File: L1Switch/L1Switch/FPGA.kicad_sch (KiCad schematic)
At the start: 34 parts, among them J11 Conn_01x06_Male, U1 XC7A35T-FTG256, X1 LFSPXO076034CUTT

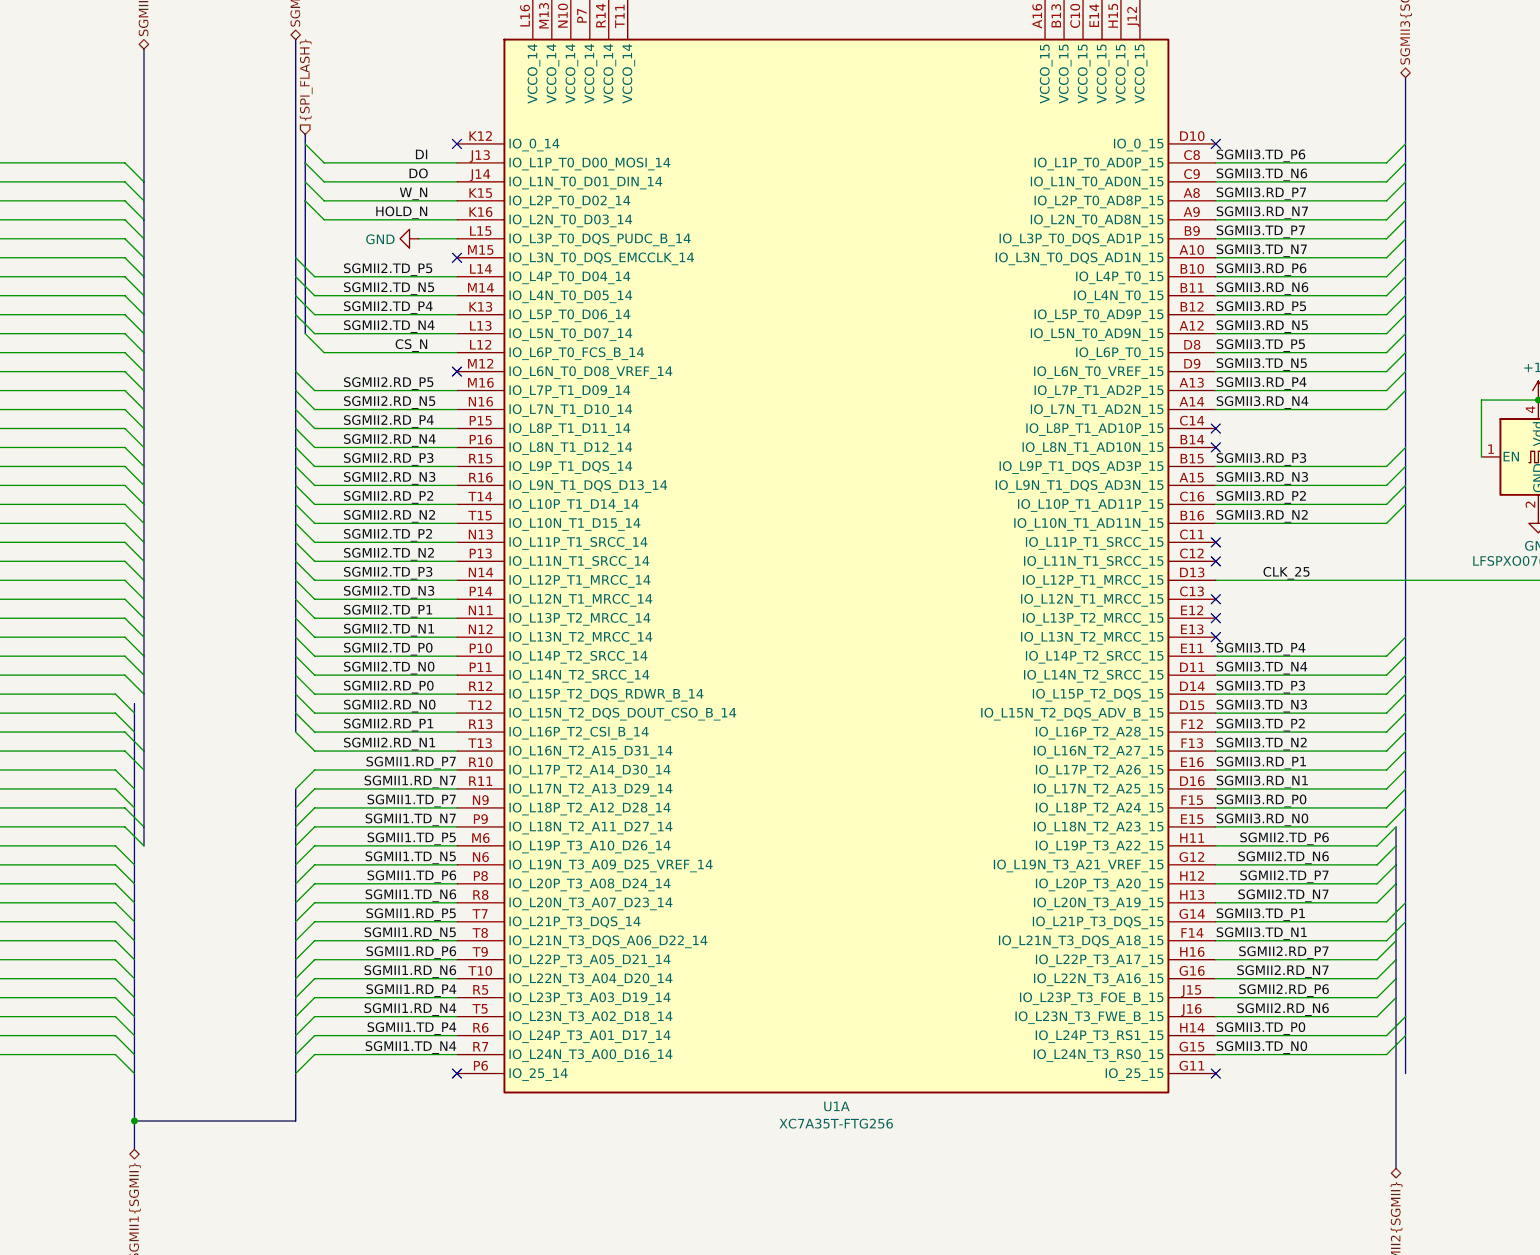
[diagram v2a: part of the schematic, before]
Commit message: Add PWR_FLAG to clean up ERC errors about undriven nets. Change R269 from 100K0 to 10K0.
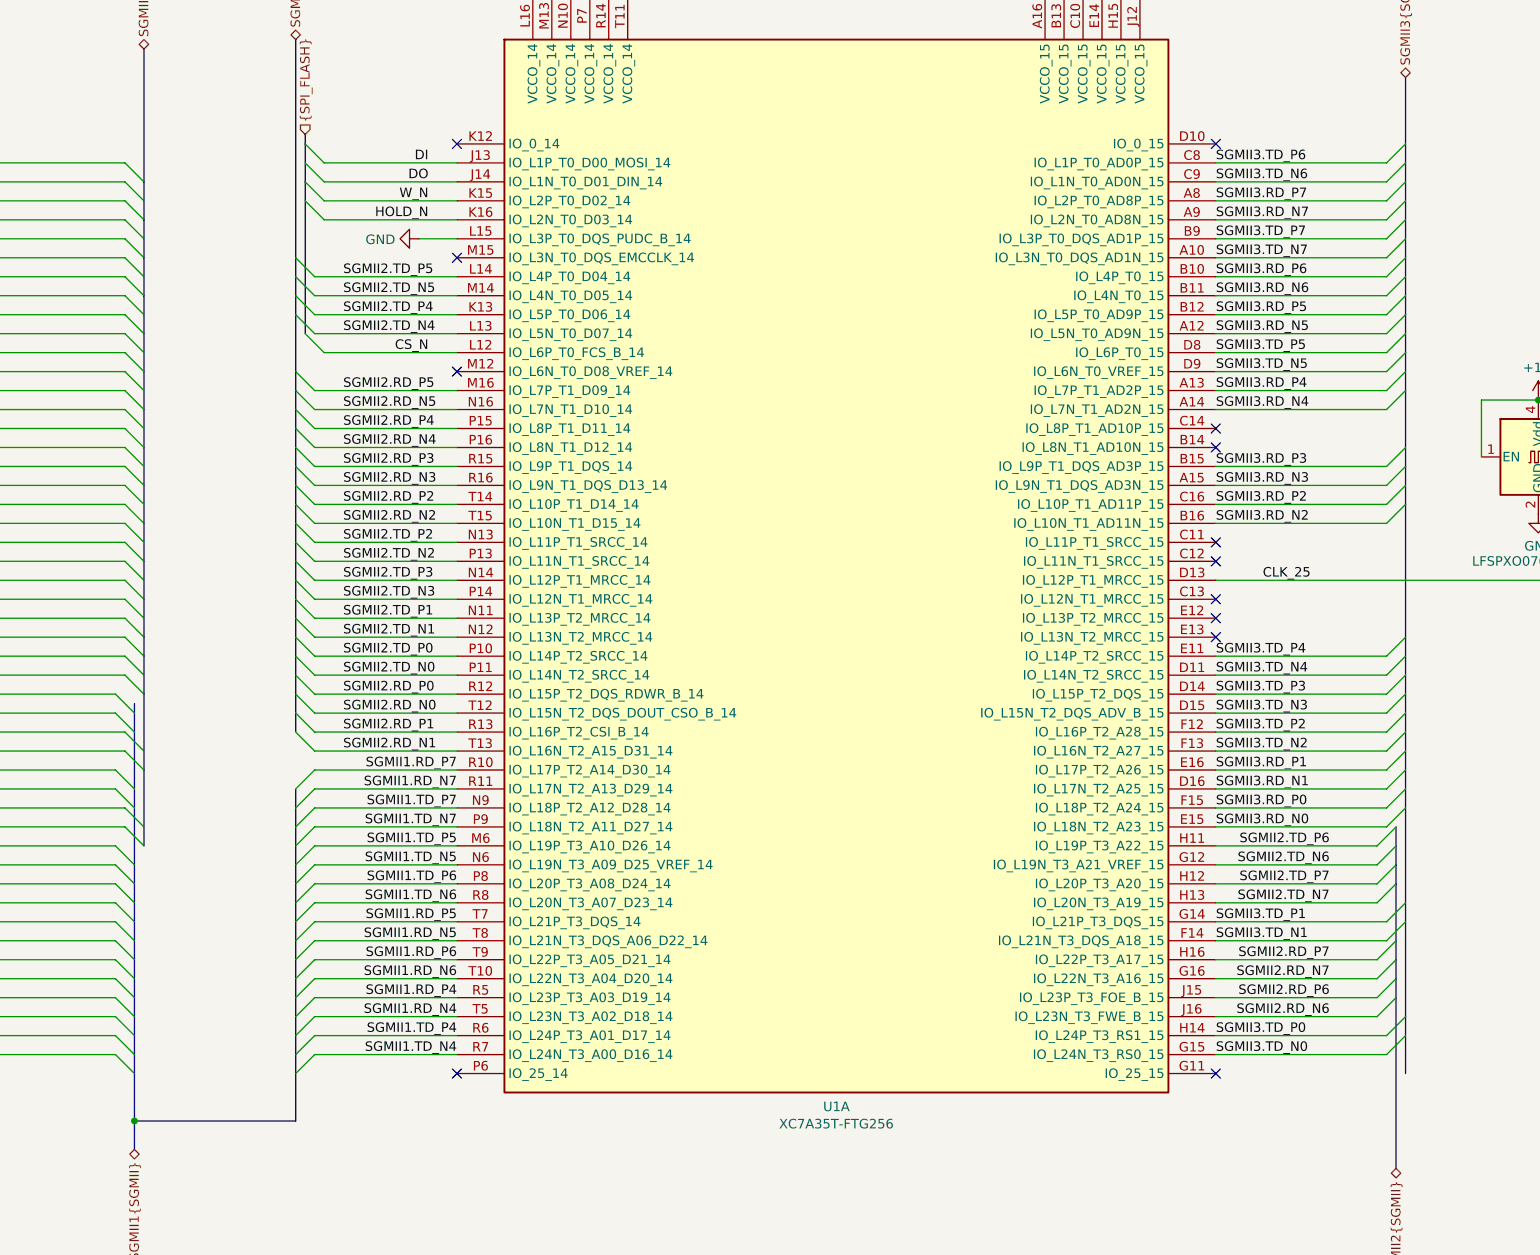
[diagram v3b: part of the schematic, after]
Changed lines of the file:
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@@
-(kicad_sch (version 20200608) (host eeschema "5.99.0-unknown-1973153~101~ubuntu20.04.1")
+(kicad_sch (version 20200608) (host eeschema "(5.99.0-1946-g60915fbc7)")
   (page 1 12)
   (paper "B")
@@
   (junction (at 414.02 125.73))
   (junction (at 213.36 198.12))
-  (no_connect (at 358.14 105.41))
-  (no_connect (at 358.14 123.19))
+  (no_connect (at 256.54 191.77))
+  (no_connect (at 256.54 82.55))
+  (no_connect (at 76.2 115.57))
   (no_connect (at 358.14 191.77))
-  (no_connect (at 76.2 102.87))
-  (no_connect (at 76.2 115.57))
-  (no_connect (at 177.8 67.31))
-  (no_connect (at 358.14 130.81))
-  (no_connect (at 256.54 67.31))
-  (no_connect (at 46.99 114.3))
-  (no_connect (at 358.14 133.35))
-  (no_connect (at 76.2 107.95))
-  (no_connect (at 358.14 120.65))
-  (no_connect (at 256.54 97.79))
-  (no_connect (at 177.8 191.77))
-  (no_connect (at 256.54 191.77))
-  (no_connect (at 76.2 105.41))
   (no_connect (at 46.99 116.84))
   (no_connect (at 358.14 128.27))
+  (no_connect (at 76.2 107.95))
+  (no_connect (at 256.54 67.31))
+  (no_connect (at 358.14 123.19))
+  (no_connect (at 358.14 105.41))
+  (no_connect (at 177.8 191.77))
+  (no_connect (at 177.8 67.31))
+  (no_connect (at 46.99 124.46))
+  (no_connect (at 358.14 120.65))
   (no_connect (at 358.14 67.31))
-  (no_connect (at 46.99 124.46))
-  (no_connect (at 256.54 82.55))
+  (no_connect (at 46.99 114.3))
+  (no_connect (at 256.54 97.79))
   (no_connect (at 358.14 107.95))
+  (no_connect (at 358.14 130.81))
+  (no_connect (at 76.2 105.41))
+  (no_connect (at 358.14 133.35))
+  (no_connect (at 76.2 102.87))
   (bus_entry (at 210.82 140.97) (size 2.54 2.54))
   (bus_entry (at 210.82 143.51) (size 2.54 2.54))
@@
     (stroke (width 0) (type solid) (color 0 0 0 0))
   )
-  (bus (pts (xy 213.36 184.15) (xy 213.36 189.23))
-    (stroke (width 0) (type solid) (color 0 0 0 0))
-  )
-  (bus (pts (xy 213.36 189.23) (xy 213.36 198.12))
+  (bus (pts (xy 213.36 184.15) (xy 213.36 186.69))
+    (stroke (width 0) (type solid) (color 0 0 0 0))
+  )
+  (bus (pts (xy 213.36 186.69) (xy 213.36 191.77))
+    (stroke (width 0) (type solid) (color 0 0 0 0))
+  )
+  (bus (pts (xy 213.36 191.77) (xy 213.36 198.12))
     (stroke (width 0) (type solid) (color 0 0 0 0))
   )
@@
     (stroke (width 0) (type solid) (color 0 0 0 0))
   )
-  (bus (pts (xy 214.63 82.55) (xy 214.63 85.09))
-    (stroke (width 0) (type solid) (color 0 0 0 0))
-  )
-  (bus (pts (xy 214.63 85.09) (xy 214.63 90.17))
-    (stroke (width 0) (type solid) (color 0 0 0 0))
-  )
-  (bus (pts (xy 214.63 90.17) (xy 214.63 95.25))
-    (stroke (width 0) (type solid) (color 0 0 0 0))
-  )
-  (bus (pts (xy 214.63 95.25) (xy 214.63 100.33))
-    (stroke (width 0) (type solid) (color 0 0 0 0))
-  )
-  (bus (pts (xy 214.63 100.33) (xy 214.63 105.41))
-    (stroke (width 0) (type solid) (color 0 0 0 0))
-  )
-  (bus (pts (xy 214.63 105.41) (xy 214.63 110.49))
-    (stroke (width 0) (type solid) (color 0 0 0 0))
-  )
-  (bus (pts (xy 214.63 110.49) (xy 214.63 115.57))
-    (stroke (width 0) (type solid) (color 0 0 0 0))
-  )
-  (bus (pts (xy 214.63 115.57) (xy 214.63 120.65))
-    (stroke (width 0) (type solid) (color 0 0 0 0))
-  )
-  (bus (pts (xy 214.63 120.65) (xy 214.63 125.73))
-    (stroke (width 0) (type solid) (color 0 0 0 0))
-  )
-  (bus (pts (xy 214.63 125.73) (xy 214.63 130.81))
-    (stroke (width 0) (type solid) (color 0 0 0 0))
-  )
-  (bus (pts (xy 214.63 130.81) (xy 214.63 135.89))
+  (bus (pts (xy 214.63 82.55) (xy 214.63 87.63))
+    (stroke (width 0) (type solid) (color 0 0 0 0))
+  )
+  (bus (pts (xy 214.63 87.63) (xy 214.63 92.71))
+    (stroke (width 0) (type solid) (color 0 0 0 0))
+  )
+  (bus (pts (xy 214.63 92.71) (xy 214.63 97.79))
+    (stroke (width 0) (type solid) (color 0 0 0 0))
+  )
+  (bus (pts (xy 214.63 97.79) (xy 214.63 102.87))
+    (stroke (width 0) (type solid) (color 0 0 0 0))
+  )
+  (bus (pts (xy 214.63 102.87) (xy 214.63 107.95))
+    (stroke (width 0) (type solid) (color 0 0 0 0))
+  )
+  (bus (pts (xy 214.63 107.95) (xy 214.63 113.03))
+    (stroke (width 0) (type solid) (color 0 0 0 0))
+  )
+  (bus (pts (xy 214.63 113.03) (xy 214.63 118.11))
+    (stroke (width 0) (type solid) (color 0 0 0 0))
+  )
+  (bus (pts (xy 214.63 118.11) (xy 214.63 123.19))
+    (stroke (width 0) (type solid) (color 0 0 0 0))
+  )
+  (bus (pts (xy 214.63 123.19) (xy 214.63 128.27))
+    (stroke (width 0) (type solid) (color 0 0 0 0))
+  )
+  (bus (pts (xy 214.63 128.27) (xy 214.63 133.35))
+    (stroke (width 0) (type solid) (color 0 0 0 0))
+  )
+  (bus (pts (xy 214.63 133.35) (xy 214.63 135.89))
     (stroke (width 0) (type solid) (color 0 0 0 0))
   )
@@
     (stroke (width 0) (type solid) (color 0 0 0 0))
   )
-  (bus (pts (xy 214.63 140.97) (xy 214.63 148.59))
-    (stroke (width 0) (type solid) (color 0 0 0 0))
-  )
-  (bus (pts (xy 214.63 148.59) (xy 214.63 158.75))
-    (stroke (width 0) (type solid) (color 0 0 0 0))
-  )
-  (bus (pts (xy 214.63 158.75) (xy 214.63 161.29))
+  (bus (pts (xy 214.63 140.97) (xy 214.63 151.13))
+    (stroke (width 0) (type solid) (color 0 0 0 0))
+  )
+  (bus (pts (xy 214.63 151.13) (xy 214.63 161.29))
     (stroke (width 0) (type solid) (color 0 0 0 0))
   )
@@
     (stroke (width 0) (type solid) (color 0 0 0 0))
   )
-  (bus (pts (xy 234.95 105.41) (xy 234.95 107.95))
-    (stroke (width 0) (type solid) (color 0 0 0 0))
-  )
-  (bus (pts (xy 234.95 107.95) (xy 234.95 113.03))
-    (stroke (width 0) (type solid) (color 0 0 0 0))
-  )
-  (bus (pts (xy 234.95 113.03) (xy 234.95 118.11))
-    (stroke (width 0) (type solid) (color 0 0 0 0))
-  )
-  (bus (pts (xy 234.95 118.11) (xy 234.95 123.19))
-    (stroke (width 0) (type solid) (color 0 0 0 0))
-  )
-  (bus (pts (xy 234.95 123.19) (xy 234.95 128.27))
-    (stroke (width 0) (type solid) (color 0 0 0 0))
-  )
-  (bus (pts (xy 234.95 128.27) (xy 234.95 133.35))
-    (stroke (width 0) (type solid) (color 0 0 0 0))
-  )
-  (bus (pts (xy 234.95 133.35) (xy 234.95 135.89))
+  (bus (pts (xy 234.95 105.41) (xy 234.95 110.49))
+    (stroke (width 0) (type solid) (color 0 0 0 0))
+  )
+  (bus (pts (xy 234.95 110.49) (xy 234.95 115.57))
+    (stroke (width 0) (type solid) (color 0 0 0 0))
+  )
+  (bus (pts (xy 234.95 115.57) (xy 234.95 120.65))
+    (stroke (width 0) (type solid) (color 0 0 0 0))
+  )
+  (bus (pts (xy 234.95 120.65) (xy 234.95 125.73))
+    (stroke (width 0) (type solid) (color 0 0 0 0))
+  )
+  (bus (pts (xy 234.95 125.73) (xy 234.95 130.81))
+    (stroke (width 0) (type solid) (color 0 0 0 0))
+  )
+  (bus (pts (xy 234.95 130.81) (xy 234.95 135.89))
     (stroke (width 0) (type solid) (color 0 0 0 0))
   )
@@
     (stroke (width 0) (type solid) (color 0 0 0 0))
   )
-  (bus (pts (xy 234.95 158.75) (xy 234.95 163.83))
-    (stroke (width 0) (type solid) (color 0 0 0 0))
-  )
-  (bus (pts (xy 234.95 163.83) (xy 234.95 168.91))
+  (bus (pts (xy 234.95 158.75) (xy 234.95 161.29))
+    (stroke (width 0) (type solid) (color 0 0 0 0))
+  )
+  (bus (pts (xy 234.95 161.29) (xy 234.95 166.37))
+    (stroke (width 0) (type solid) (color 0 0 0 0))
+  )
+  (bus (pts (xy 234.95 166.37) (xy 234.95 168.91))
     (stroke (width 0) (type solid) (color 0 0 0 0))
   )
@@
     (stroke (width 0) (type solid) (color 0 0 0 0))
   )
-  (bus (pts (xy 236.22 66.04) (xy 236.22 69.85))
-    (stroke (width 0) (type solid) (color 0 0 0 0))
-  )
-  (bus (pts (xy 236.22 69.85) (xy 236.22 74.93))
-    (stroke (width 0) (type solid) (color 0 0 0 0))
-  )
-  (bus (pts (xy 236.22 74.93) (xy 236.22 92.71))
+  (bus (pts (xy 236.22 66.04) (xy 236.22 67.31))
+    (stroke (width 0) (type solid) (color 0 0 0 0))
+  )
+  (bus (pts (xy 236.22 67.31) (xy 236.22 72.39))
+    (stroke (width 0) (type solid) (color 0 0 0 0))
+  )
+  (bus (pts (xy 236.22 72.39) (xy 236.22 92.71))
     (stroke (width 0) (type solid) (color 0 0 0 0))
   )
@@
     (stroke (width 0) (type solid) (color 0 0 0 0))
   )
-  (bus (pts (xy 383.54 151.13) (xy 383.54 156.21))
-    (stroke (width 0) (type solid) (color 0 0 0 0))
-  )
-  (bus (pts (xy 383.54 156.21) (xy 383.54 168.91))
-    (stroke (width 0) (type solid) (color 0 0 0 0))
-  )
+  (bus (pts (xy 383.54 151.13) (xy 383.54 153.67))
+    (stroke (width 0) (type solid) (color 0 0 0 0))
+  )
+  (bus (pts (xy 383.54 153.67) (xy 383.54 168.91))
+    (stroke (width 0) (type solid) (color 0 0 0 0))
+  )
